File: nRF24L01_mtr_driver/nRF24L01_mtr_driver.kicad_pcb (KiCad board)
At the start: 4 copper layers, 60.1 x 39.9 mm, 147 parts, among them J1 Micro USB, J2 I/O, J4 VBAT, J5 MTR, J6 SERVO, J7 ICSP, Q1 AO4484, Q2 AO4484, Q3 AO4484, Q4 AO4484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

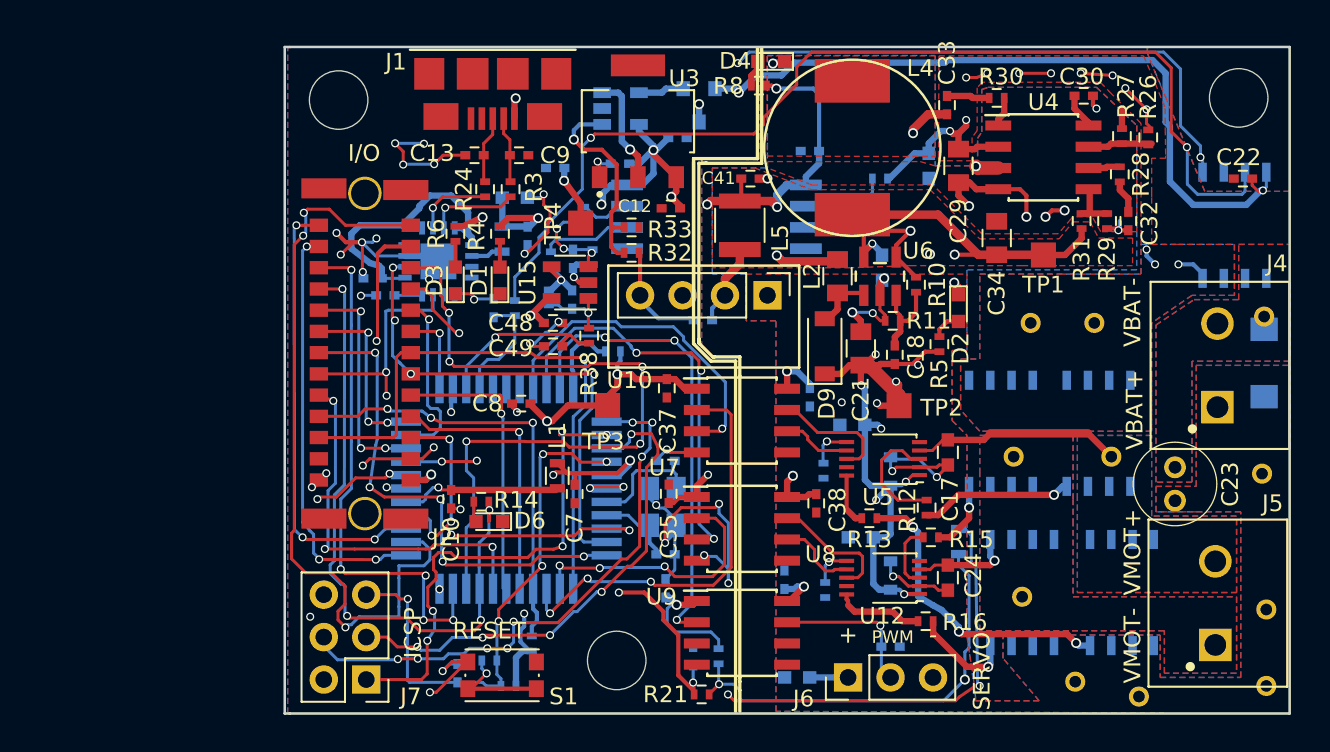
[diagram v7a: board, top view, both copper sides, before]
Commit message: silkscreen touch-up done, added AMS117 and Block Term 3D models
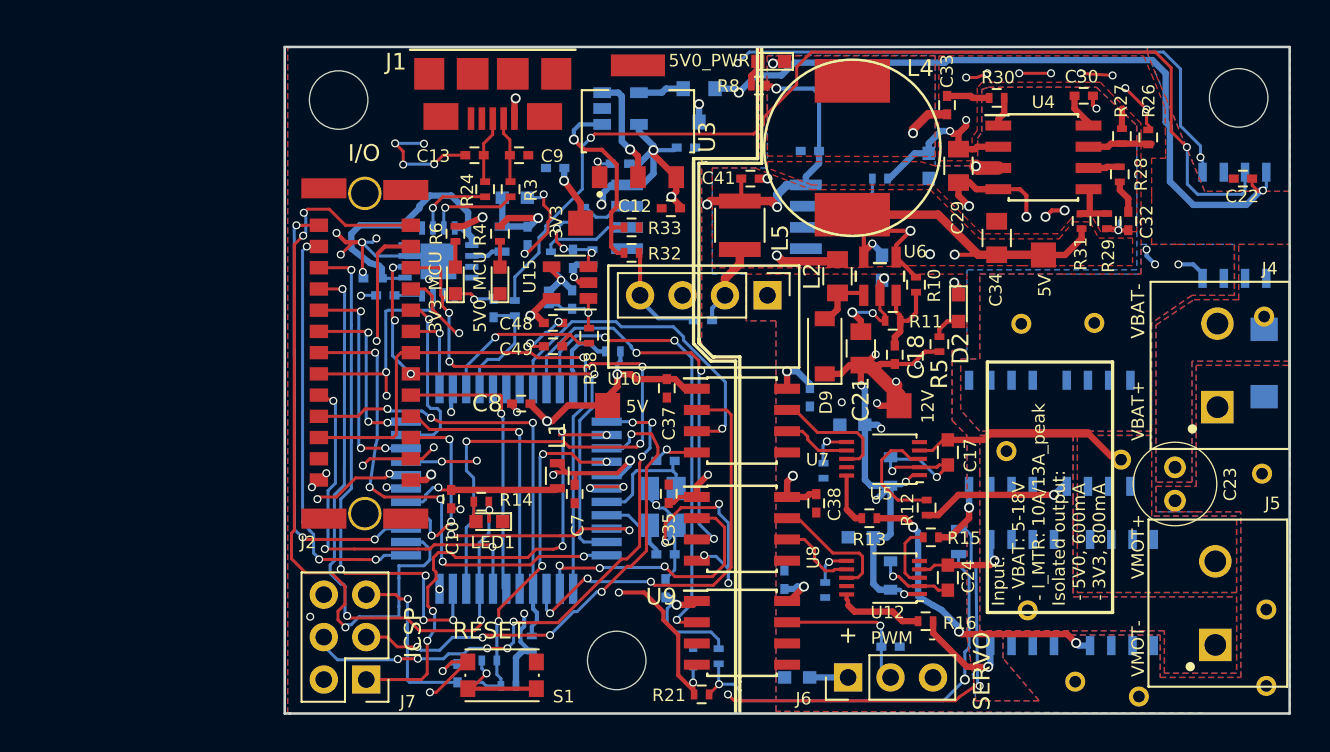
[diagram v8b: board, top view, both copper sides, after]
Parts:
- moved REF** 0.88 mm to (105.4, 78.7)
- moved C43 0.76 mm to (84.9, 51.0)
- moved REF** 0.61 mm to (110.9, 69.6)
- moved REF** 0.56 mm to (105.0, 61.5)
- moved REF** 0.54 mm to (104.1, 69.1)
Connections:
- J1 pad : (no net) -> GNDA
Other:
- board text added: "12V"
- board text added: "3V3"
- board text added: "3V3_MCU"
- board text added: "5V"
- board text added: "5V0_MCU"
- board text added: "5V0_PWR"
- board text added: "Input: - VBAT: 5-18V - I_MTR: 10A/13A_peak Isolated output: - 5V0, 600mA - 3V3, 800mA"
- board text added: "LED1"
